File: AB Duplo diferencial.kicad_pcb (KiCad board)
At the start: 2 copper layers, 44 parts, among them Q1 C945, Q10 13007, Q11 13007, Q2 C945, Q3 A733, Q4 A733, Q5 A733, Q6 13003, Q7 C945, Q8 TIP41, Q9 TIP42

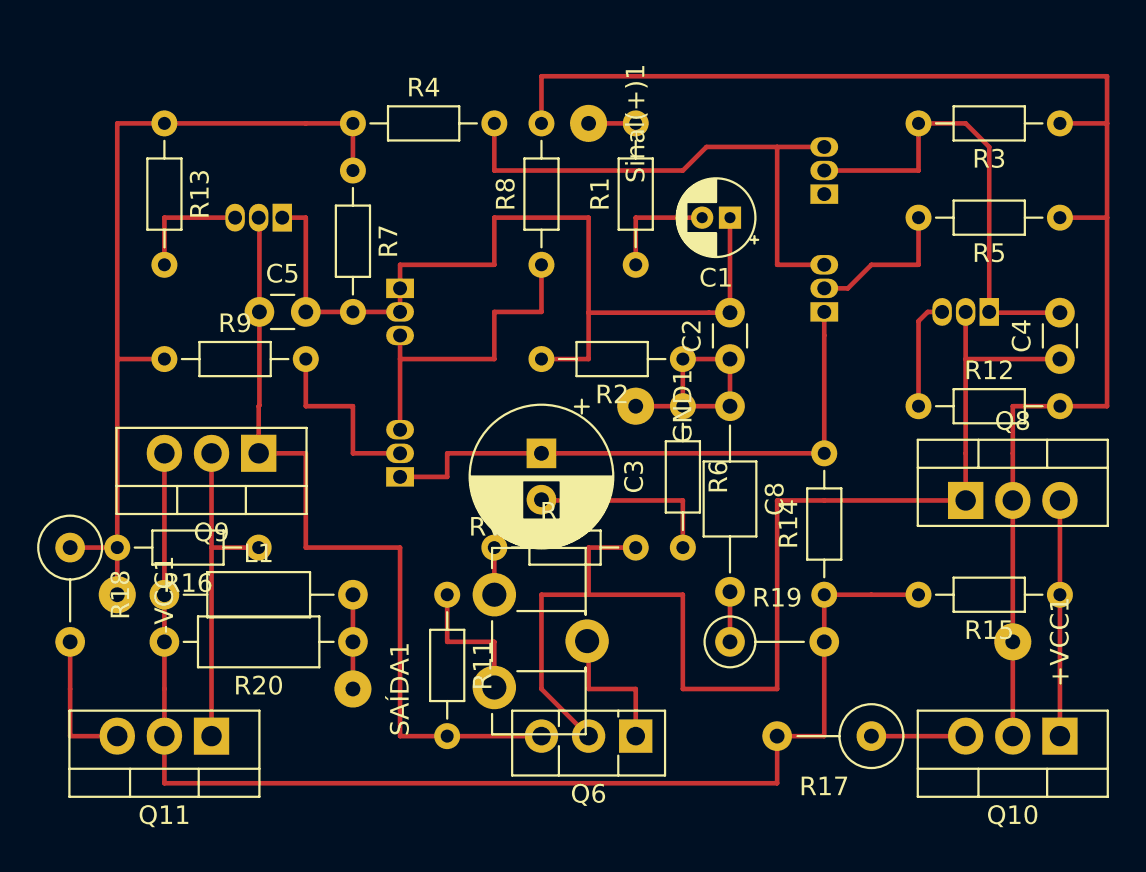
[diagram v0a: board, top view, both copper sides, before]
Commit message: Otimizadas algumas trilhas & adicionado resistor 4.7k da entrada pro terra para reduzir o ruído de 60hz
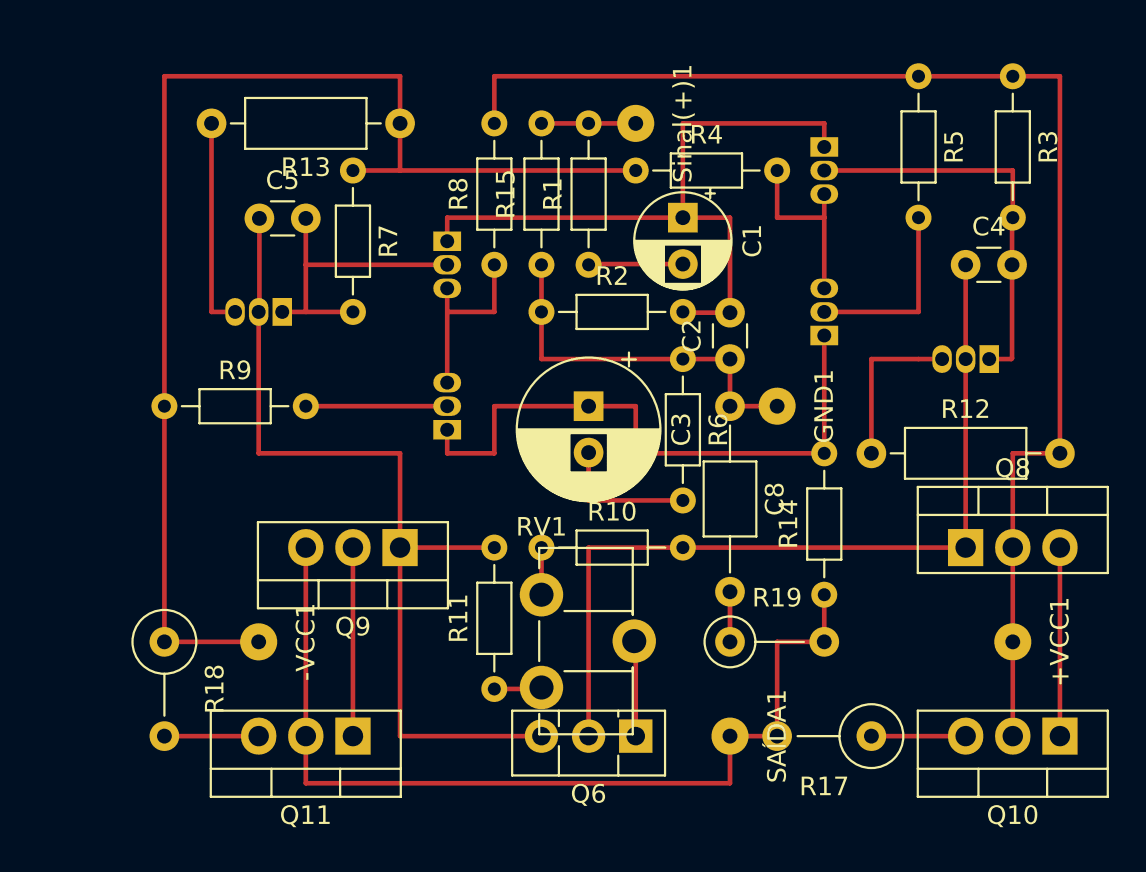
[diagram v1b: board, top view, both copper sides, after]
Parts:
- removed L1: L_Small, Inductor_THT:L_Axial_L5.3mm_D2.2mm_P10.16mm_Horizontal_Vishay_IM-1
- removed R16: 100R, Resistor_THT:R_Axial_DIN0204_L3.6mm_D1.6mm_P7.62mm_Horizontal
- removed R20: 10r, Resistor_THT:R_Axial_DIN0207_L6.3mm_D2.5mm_P10.16mm_Horizontal
- C1: footprint Capacitor_THT:CP_Radial_D4.0mm_P1.50mm -> Capacitor_THT:CP_Radial_D5.0mm_P2.50mm
- R12, R13: value 10r -> 1k; footprint Resistor_THT:R_Axial_DIN0204_L3.6mm_D1.6mm_P7.62mm_Horizontal -> Resistor_THT:R_Axial_DIN0207_L6.3mm_D2.5mm_P10.16mm_Horizontal
- R15: value 100R -> 4,7k
- moved R15 33.1 mm to (81.3, 35.6), turned to 90 degrees
- moved SAÍDA1 20.5 mm to (91.4, 61.0)
- moved R4 15.5 mm to (86.4, 30.5)
- moved R13 12.7 mm to (73.7, 27.9), turned to 180 degrees
- moved R5 10.8 mm to (101.6, 25.4), turned to 270 degrees
- moved Q9 9.16 mm to (73.7, 50.8)
- moved -VCC1 8.03 mm to (66.0, 55.9)
- moved R2 8.03 mm to (81.3, 38.1), turned to 0 degrees
- moved GND1 7.62 mm to (94.0, 43.2)
- moved Q11 7.62 mm to (71.1, 61.0)
- moved R18 7.18 mm to (61.0, 55.9)
- moved C4 7.18 mm to (104.1, 35.6), turned to 0 degrees
- moved R11 5.68 mm to (78.7, 58.4), turned to 90 degrees
- moved Q7 5.08 mm to (67.3, 38.1)
- moved C5 5.04 mm to (66.1, 33.1)
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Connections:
- R15 pad 1: Net-(Q10-Pad1) -> Earth
- R15 pad 2: Net-(L1-Pad1) -> Net-(R1-Pad2)
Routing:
- net Net-(-VCC1-Pad1): track 45.7 -> 68.6 mm
- net Net-(C4-Pad1): track 67.1 -> 45.7 mm
- net Net-(Q1-Pad3): track 29.7 -> 10.2 mm
- net Net-(L1-Pad1): track 68.6 -> 50.8 mm
- net Net-(Q3-Pad3): track 17.8 -> 10.2 mm
- net Net-(+VCC1-Pad1): track 78.7 -> 71.1 mm
- net Earth: track 12.7 -> 20.3 mm
- net Net-(Q11-Pad1): track 17.8 -> 10.2 mm
- net Net-(C5-Pad2): track 11.0 -> 16.5 mm
- net Net-(Q7-Pad3): track 6.35 -> 11.4 mm
- net Net-(L1-Pad2): track 5.08 -> 0.00 mm
- net Net-(C5-Pad1): track 43.3 -> 48.2 mm
- net Net-(R11-Pad1): track 7.54 -> 2.69 mm
- net Net-(C4-Pad2): track 24.6 -> 21.5 mm
- net Net-(Q5-Pad3): track 6.06 -> 8.89 mm
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
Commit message: Alteradas rotas para R7 e R11 & expandido placa geral 1 furo para esquerda
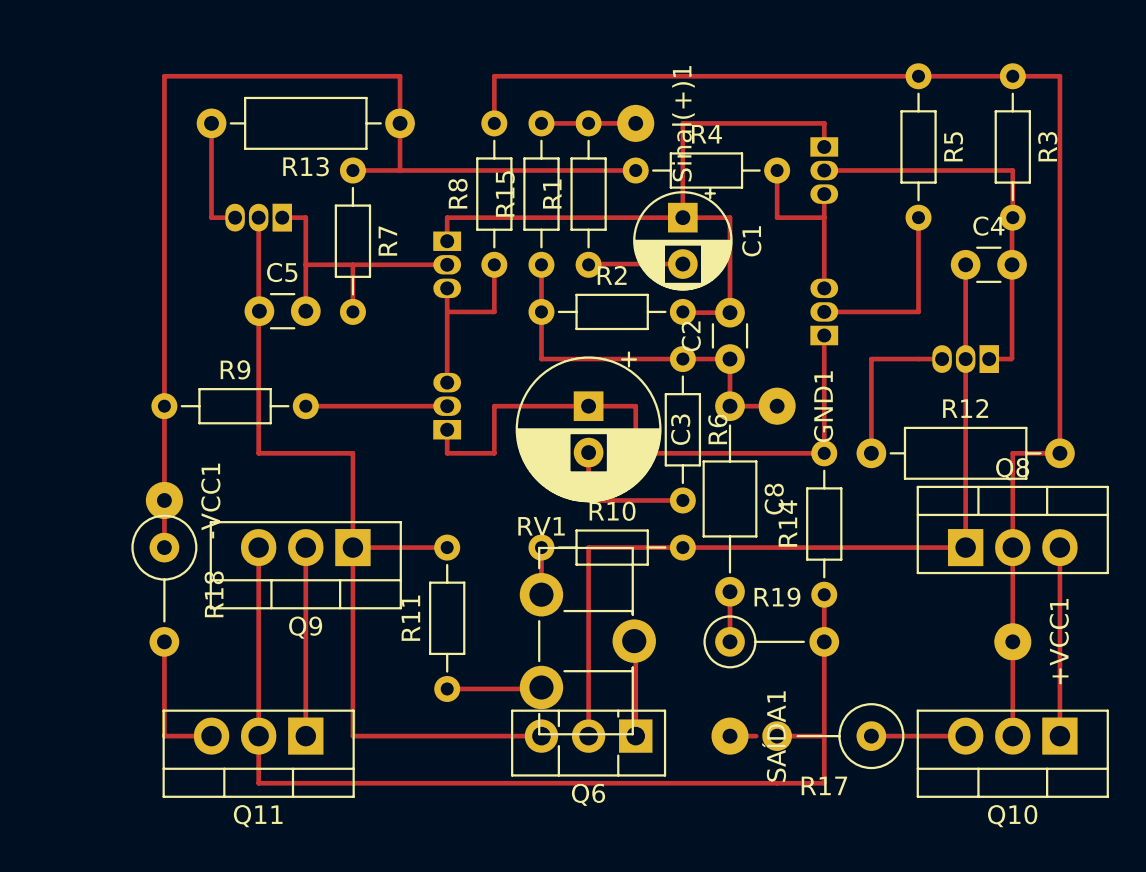
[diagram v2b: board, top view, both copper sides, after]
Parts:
- moved -VCC1 9.16 mm to (61.0, 48.3)
- moved R18 5.08 mm to (61.0, 50.8)
- moved Q7 5.08 mm to (67.3, 33.0)
- moved C5 5.00 mm to (66.1, 38.1)
- moved Q11 2.54 mm to (68.6, 61.0)
- moved Q9 2.54 mm to (71.1, 50.8)
- moved R11 2.54 mm to (76.2, 58.4)
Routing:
- net Net-(-VCC1-Pad1): track 68.6 -> 58.4 mm
- net Net-(L1-Pad1): track 50.8 -> 55.9 mm
- net Net-(Q7-Pad3): track 11.4 -> 6.35 mm
- net Net-(Q11-Pad3): track 5.08 -> 7.62 mm
- net Net-(R11-Pad1): track 2.69 -> 5.11 mm
- net Net-(L1-Pad2): track 0.00 -> 1.41 mm

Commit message: Reordenação de 20 para 17 linhas na vertical para encaixar dois projetos em uma placa de 15x34
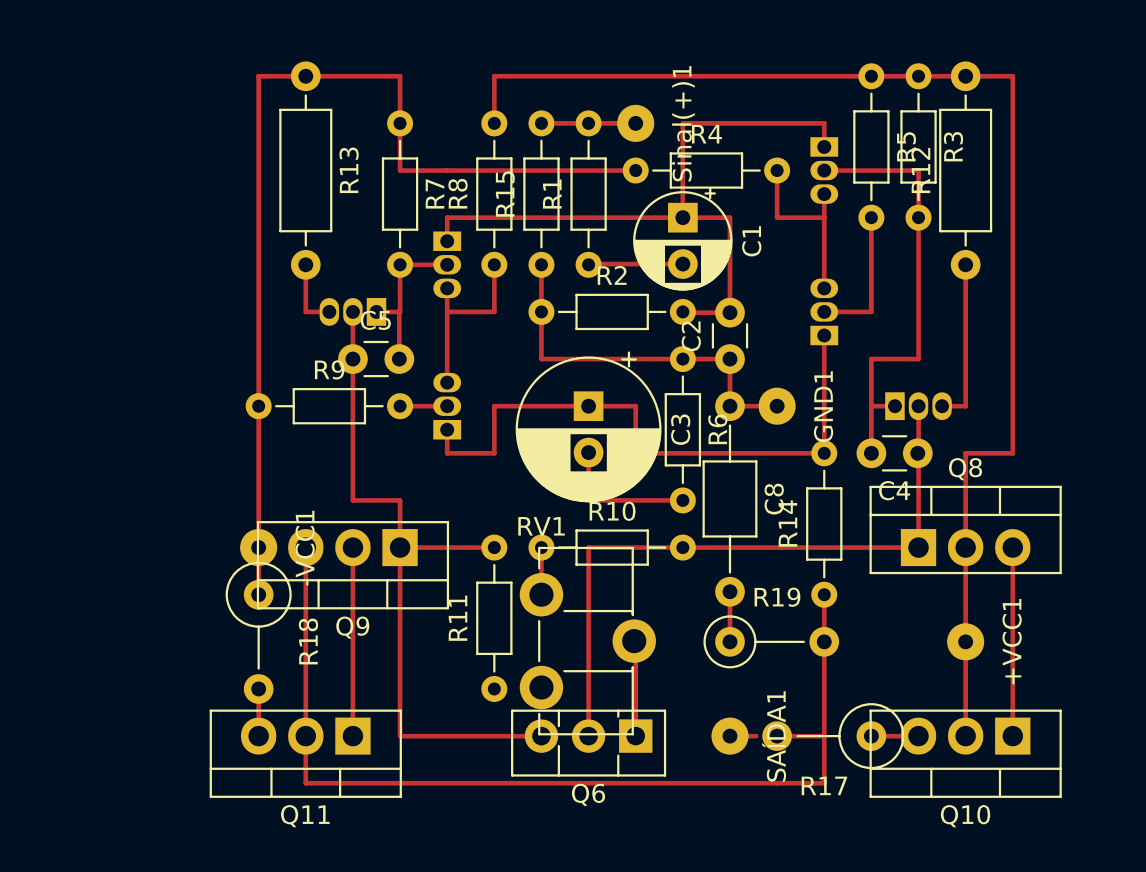
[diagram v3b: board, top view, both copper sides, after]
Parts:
- moved R12 11.4 mm to (104.1, 35.6), turned to 90 degrees
- moved C4 10.5 mm to (101.6, 45.7), turned to 180 degrees
- moved Q7 7.18 mm to (72.4, 38.1)
- moved R18 5.68 mm to (66.0, 53.3)
- moved -VCC1 5.68 mm to (66.0, 50.8)
- moved R13 5.68 mm to (68.6, 25.4), turned to 270 degrees
- moved Q5 5.68 mm to (100.3, 43.2), turned to 0 degrees
- moved C5 5.66 mm to (71.1, 40.6)
- moved R3 5.08 mm to (101.6, 25.4)
- moved R9 5.08 mm to (66.0, 43.2)
- moved R7 3.59 mm to (73.7, 27.9)
- moved +VCC1 2.54 mm to (104.1, 55.9)
- moved Q11 2.54 mm to (71.1, 61.0)
- moved Q8 2.54 mm to (101.6, 50.8)
- moved Q10 2.54 mm to (106.7, 61.0)
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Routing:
- net Net-(C5-Pad1): track 48.3 -> 38.1 mm
- net Net-(C4-Pad1): track 45.7 -> 35.6 mm
- net Net-(C5-Pad2): track 16.5 -> 8.91 mm
- net Net-(Q4-Pad2): track 7.62 -> 2.54 mm
- net Net-(-VCC1-Pad1): track 58.4 -> 53.3 mm
- net Net-(Q11-Pad3): track 7.62 -> 2.59 mm
- net Net-(R11-Pad1): track 5.11 -> 0.11 mm
- net Net-(L1-Pad1): track 55.9 -> 53.3 mm
- net Net-(C4-Pad2): track 21.5 -> 24.1 mm
- net Net-(Q10-Pad3): track 5.08 -> 2.54 mm
- net Net-(Q7-Pad3): track 6.35 -> 3.81 mm
- net Net-(Q2-Pad2): track 10.2 -> 7.62 mm
- net Net-(+VCC1-Pad1): track 71.1 -> 68.6 mm

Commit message: [trocados de posição] C4 e Q5, C5 e Q7 para que a filtragem do capacitor venha antes da base [otimizado] R5 direto para Q2 [rotacionado] R3 para mesma orientação de R5 [encurtado] trilha entre -VCC e R4
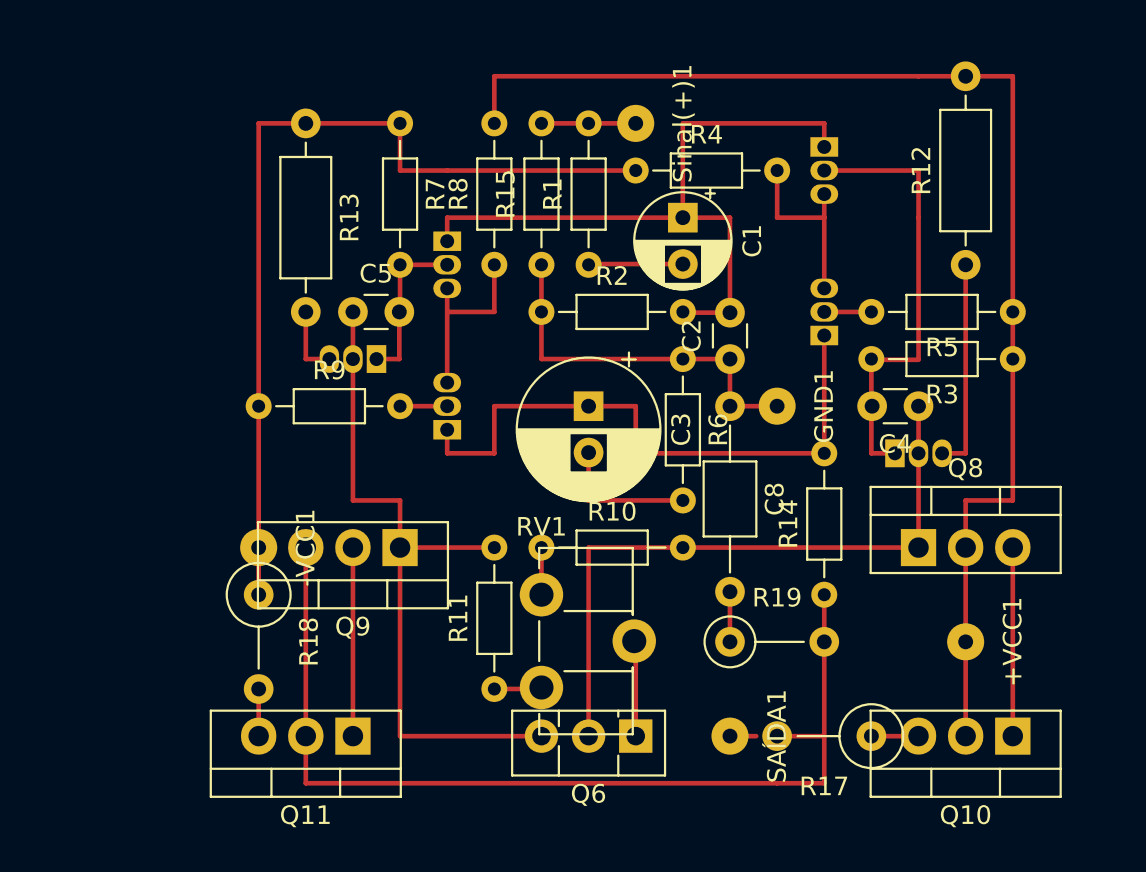
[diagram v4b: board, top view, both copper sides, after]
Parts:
- moved R3 16.1 mm to (106.7, 40.6), turned to 180 degrees
- moved R5 14.8 mm to (106.7, 38.1), turned to 180 degrees
- moved C4 2.54 mm to (101.6, 43.2)
- moved R13 2.54 mm to (68.6, 27.9)
- moved C5 2.54 mm to (71.1, 38.1)
- moved Q5 2.54 mm to (100.3, 45.7)
- moved Q7 2.54 mm to (72.4, 40.6)
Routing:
- net Net-(-VCC1-Pad1): track 53.3 -> 48.3 mm
- net Net-(Q2-Pad2): track 7.62 -> 2.54 mm
- net Net-(Q5-Pad3): track 8.89 -> 11.4 mm
- net Net-(R11-Pad1): track 0.11 -> 2.57 mm

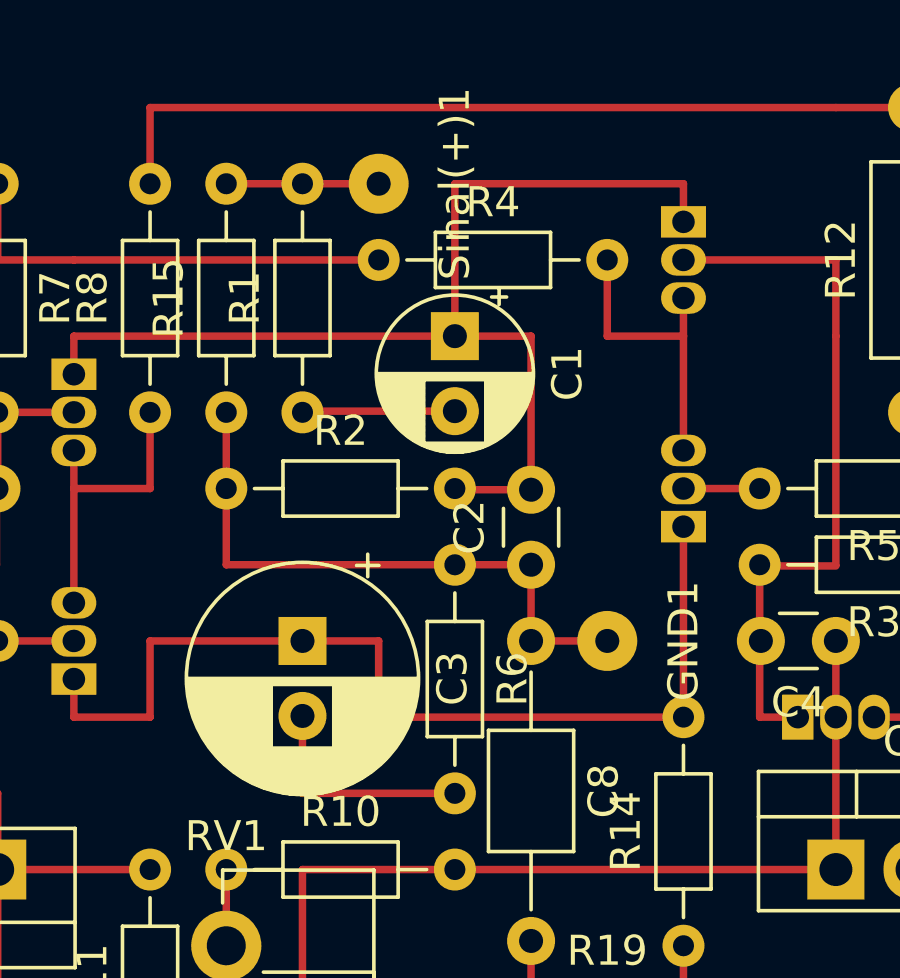
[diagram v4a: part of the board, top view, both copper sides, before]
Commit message: [centralizados]  Nomes nos próprios componentes do pcb
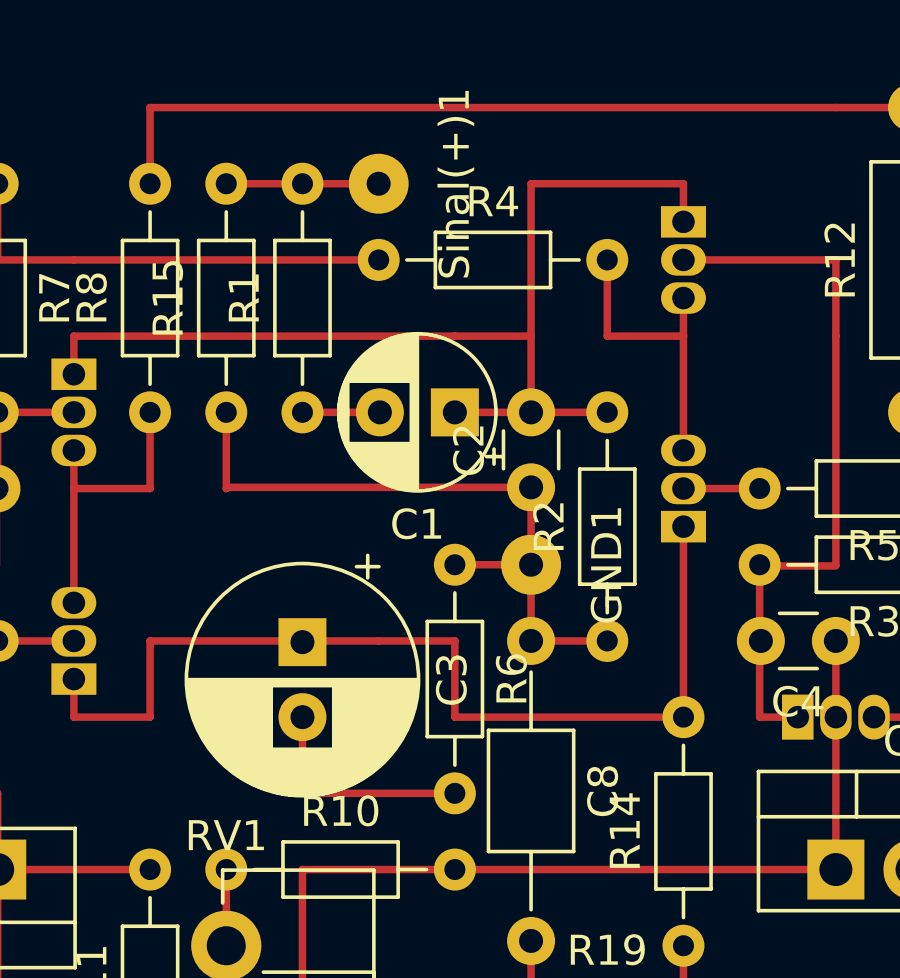
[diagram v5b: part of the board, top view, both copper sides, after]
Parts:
- moved R2 13.7 mm to (94.0, 43.2), turned to 90 degrees
- moved GND1 3.59 mm to (91.4, 40.6)
- moved C2 2.58 mm to (91.4, 38.1)
- moved C1 2.54 mm to (88.9, 35.6), turned to 180 degrees
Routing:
- net Net-(C1-Pad1): track 38.2 -> 35.6 mm
- net Earth: track 20.3 -> 22.9 mm
- net Net-(C1-Pad2): track 5.10 -> 2.69 mm

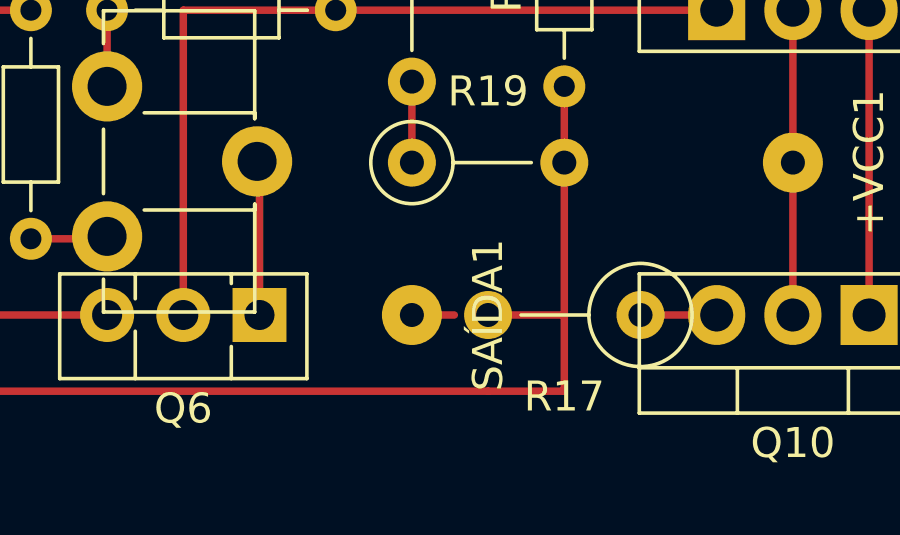
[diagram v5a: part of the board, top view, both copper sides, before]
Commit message: [atualizados] Valores: C7(47uf) & R2/R14(100k) & R12/R13(2K) & R15(10K) [renomeados] "Sinal(+)" para "P2" & +VCC1 para "+24" & "-VCC1" para "-24" & "SAÍDA" para "Falante"
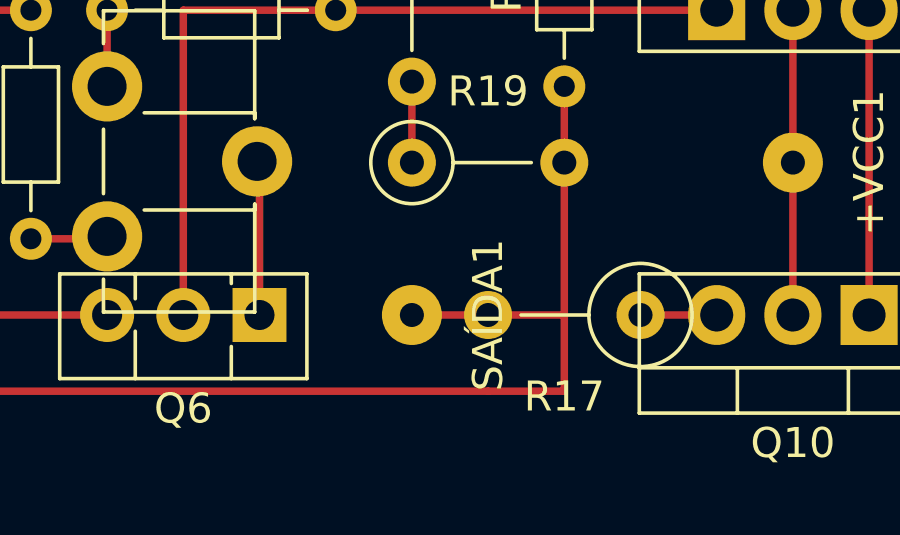
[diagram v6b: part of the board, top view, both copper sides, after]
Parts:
- +VCC1: value +VCC -> +24
- -VCC1: value -VCC -> -24
- C3: value 100uf -> 47uf
- C4, C5: value 47pf -> 100pf
- Q6: value 13003 -> C945
- R12, R13: value 1k -> 2k
- R14, R2: value 47k -> 100k
- R15: value 4,7k -> 10k
- SAÍDA1: value SAÍDA -> Falante
- Sinal(+)1: value Sinal(+) -> P2(+)
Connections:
- Q11 pad 2: Net-(L1-Pad1) -> Net-(Q11-Pad2)
- Q9 pad 3: Net-(L1-Pad1) -> Net-(Q11-Pad2)
- R14 pad 1: Net-(L1-Pad1) -> Net-(Q11-Pad2)
- R17 pad 2: Net-(L1-Pad1) -> Net-(Q11-Pad2)
- R19 pad 2: Net-(L1-Pad1) -> Net-(Q11-Pad2)
- SAÍDA1 pad 1: Net-(L1-Pad2) -> Net-(Q11-Pad2)
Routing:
- net Net-(Q11-Pad2): track 0.00 -> 55.9 mm
- net Net-(L1-Pad1): track 53.3 -> 0.00 mm
- net Net-(L1-Pad2): track 1.41 -> 0.00 mm
